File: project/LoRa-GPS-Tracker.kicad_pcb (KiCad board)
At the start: 2 copper layers, 38.9 x 40 mm, 47 parts, among them IC1 MCP73831-2-OT, IC103 FT230XS, IC104 NCP705MT30TCG, IC2 MCP100-300D, M1 SIM28ML, M102 RAK3172, Q101 BSS123, Q102 TP0610K, Q103 BSH205G2VL, SW101 ON / OFF, X1 USB_B_Micro, X103 +, X104 -, X3 Conn_Coaxial

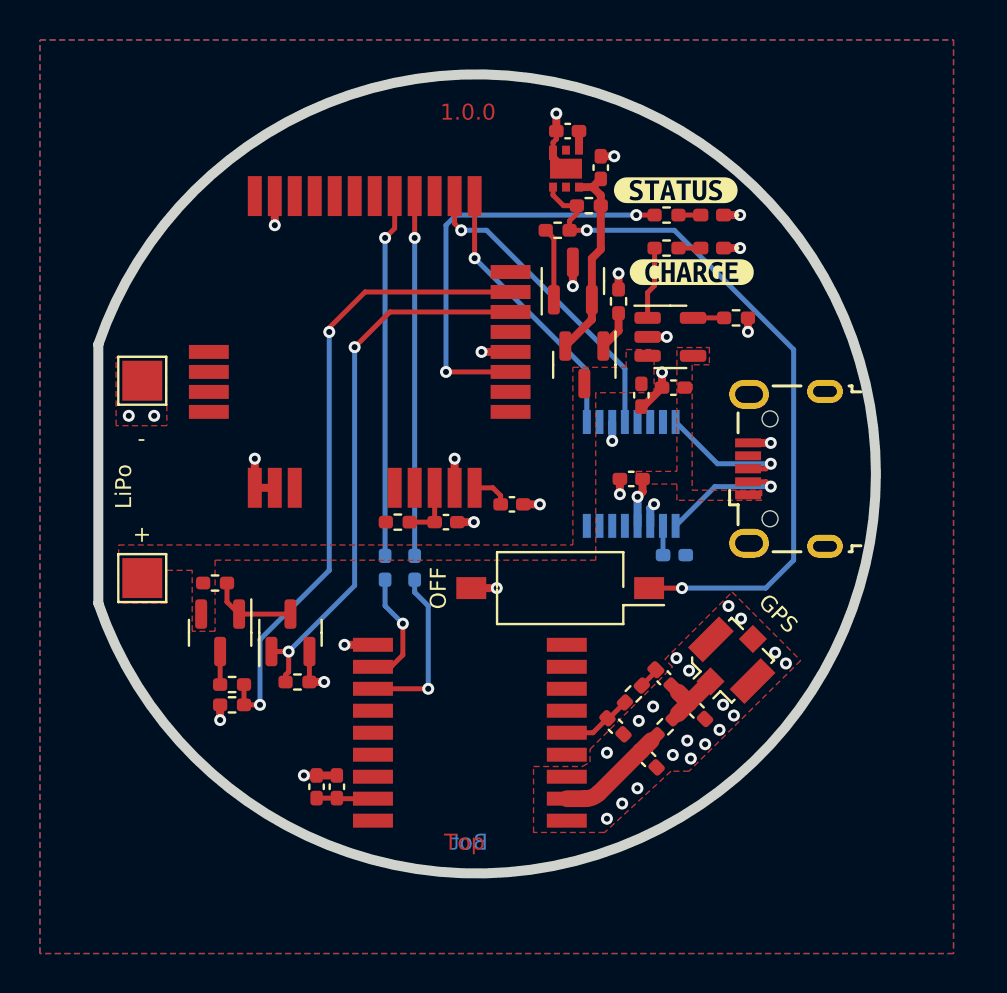
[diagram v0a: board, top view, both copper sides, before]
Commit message: Version 1
PCB:
- Update build.yaml
- Add PCB variant for KiBot

Signed-off-by: Daniel Kampert <DanielKampert@kampis-elektroecke.de>
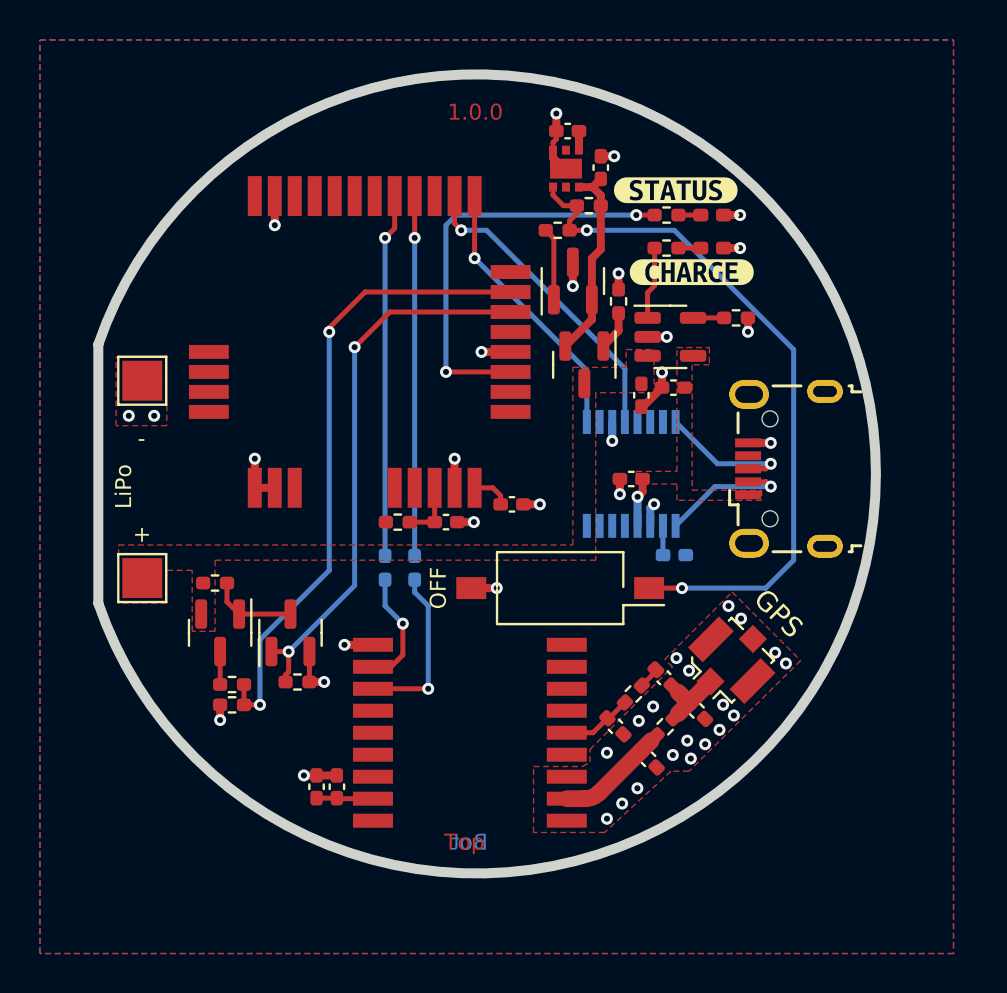
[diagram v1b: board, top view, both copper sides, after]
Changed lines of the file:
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@@
   (paper "A4")
   (title_block
-    (title "LoRa-Weatherstation")
-    (date "2022-12-31")
+    (title "LoRa-GPS-Tracker")
+    (date "2024-01-07")
     (rev "1.0")
     (company "Kampis-Elektroecke")
@@
         (effects (font (size 1 1) (thickness 0.15)))
     )
-    (fp_text user "${REFERENCE}" (at 0 0 90) (layer "F.Fab")
+    (fp_text user "${REFERENCE}" (at 0 0 -180) (layer "F.Fab")
         (effects (font (size 0.32 0.32) (thickness 0.05)))
     )
@@
         (effects (font (size 1 1) (thickness 0.15)))
     )
-    (fp_text user "${REFERENCE}" (at 0 0) (layer "F.Fab")
+    (fp_text user "${REFERENCE}" (at 0 0 90) (layer "F.Fab")
         (effects (font (size 1 1) (thickness 0.15)))
     )
@@
         (effects (font (size 1 1) (thickness 0.15)))
     )
-    (fp_text user "${REFERENCE}" (at 0 0) (layer "F.Fab")
+    (fp_text user "${REFERENCE}" (at 0 0 90) (layer "F.Fab")
         (effects (font (size 0.4 0.4) (thickness 0.06)))
     )
@@
         (effects (font (size 1 1) (thickness 0.15)))
     )
-    (fp_text user "${REFERENCE}" (at 0 0 90) (layer "F.Fab")
+    (fp_text user "${REFERENCE}" (at 0 0 180) (layer "F.Fab")
         (effects (font (size 0.32 0.32) (thickness 0.05)))
     )
@@
         (effects (font (size 1 1) (thickness 0.15)))
     )
-    (fp_text user "${REFERENCE}" (at 0 0 90) (layer "F.Fab")
+    (fp_text user "${REFERENCE}" (at 0 0 -180) (layer "F.Fab")
         (effects (font (size 0.32 0.32) (thickness 0.05)))
     )
@@
         (effects (font (size 1 1) (thickness 0.15)))
     )
-    (fp_text user "${REFERENCE}" (at 0.1 0 180 unlocked) (layer "F.Fab")
+    (fp_text user "${REFERENCE}" (at 0.1 0 unlocked) (layer "F.Fab")
         (effects (font (size 0.6 0.6) (thickness 0.09)))
     )
@@
         (effects (font (size 1 1) (thickness 0.15)))
     )
-    (fp_text user "${REFERENCE}" (at 0 0 90) (layer "F.Fab")
+    (fp_text user "${REFERENCE}" (at 0 0 180) (layer "F.Fab")
         (effects (font (size 0.32 0.32) (thickness 0.05)))
     )
@@
         (effects (font (size 1 1) (thickness 0.15)))
     )
-    (fp_text value "GPS" (at -0.006364 -3.295881 135) (layer "F.SilkS")
-        (effects (font (size 0.8 0.8) (thickness 0.1)))
+    (fp_text value "GPS" (at 0 -3.302 135) (layer "F.SilkS")
+        (effects (font (size 1 1) (thickness 0.15)))
     )
     (fp_text user "${REFERENCE}" (at 0 0 135) (layer "F.Fab")
@@
   (gr_arc (start 124.901 99.72) (mid 163.816029 106.197) (end 124.901 112.674)
     (stroke (width 0.5) (type solid)) (layer "Edge.Cuts"))
-  (gr_text "1.0.0" (at 143.4 88.1) (layer "F.Cu")
+  (gr_text "1.0.0" (at 143.766 88.1) (layer "F.Cu")
     (effects (font (size 0.8 0.8) (thickness 0.12)))
   )

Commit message: Version 1.0
Electronics:
- Add jumper for current measurement
- Add jumper to set the RAK module into bootloader mode
- Add capacitor for battery measurement

Testing Firmware:
- Add UART GPS parser
- SubGHz PHY is now using the coordinates from GPS

Firmware:
- Add STM32CubeMX project

Misc:
- Add README

- Add CHANGELOG

Signed-off-by: Daniel Kampert <DanielKampert@kampis-elektroecke.de>
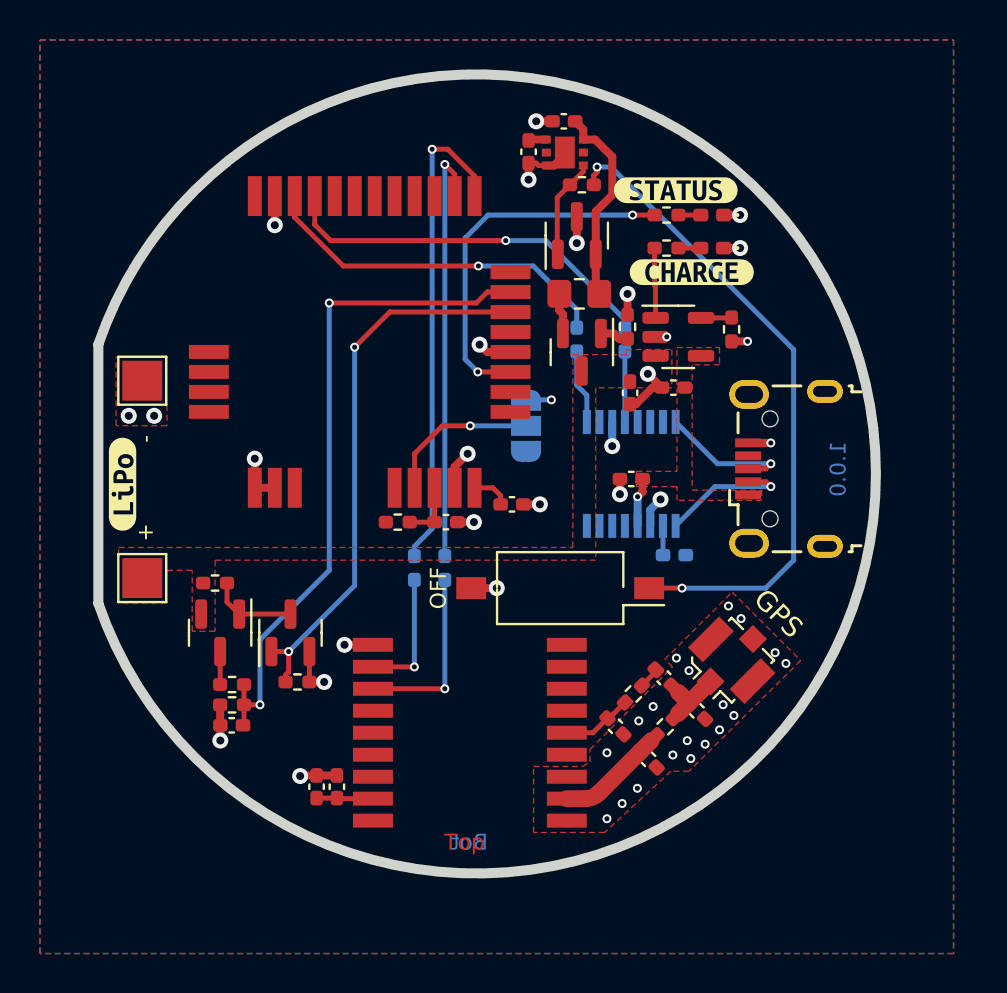
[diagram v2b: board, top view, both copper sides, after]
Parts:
- added C103: 100n, Capacitor_SMD:C_0402_1005Metric_Pad0.74x0.62mm_HandSolder, F.Cu at (131.6, 118.8)
- added JP101: PROG, Jumper:SolderJumper-3_P1.3mm_Open_RoundedPad1.0x1.5mm_NumberLabels, B.Cu at (146.3, 103.8)
- added R114: 0R, Resistor_SMD:R_0402_1005Metric_Pad0.72x0.64mm_HandSolder, B.Cu at (148.8, 99.5)
- added R115: 0R, Resistor_SMD:R_0402_1005Metric_Pad0.72x0.64mm_HandSolder, B.Cu at (151.3, 99.5)
- added kibuzzard-659DAEA0: G***, kibuzzard-659DAEA0, F.Cu at (126.1, 106.7)
- R101, R102: value 100R -> 0R
- R112: value 3k3 -> 0R; footprint Resistor_SMD:R_0402_1005Metric_Pad0.72x0.64mm_HandSolder -> Resistor_SMD:R_0805_2012Metric_Pad1.20x1.40mm_HandSolder
- moved R112 3.36 mm to (149.0, 97.2), turned to 180 degrees
- moved C111 2.96 mm to (148.2, 88.6), turned to 180 degrees
- moved IC2 2.29 mm to (148.8, 94.3)
- moved C112 2.21 mm to (146.4, 90.1), turned to -90 degrees
- moved R102 1.51 mm to (142.2, 110.9)
- moved R101 1.47 mm to (140.7, 110.9)
- moved R111 1.35 mm to (151.4, 98.8)
- moved R113 1.10 mm to (149.1, 91.7), turned to 0 degrees
- moved IC104 0.81 mm to (148.2, 90.1), turned to -90 degrees
- moved Q103 0.64 mm to (149.1, 100.1)
- moved R107 0.62 mm to (156.6, 99.0), turned to -90 degrees
- moved C108 0.58 mm to (151.5, 102.1)
- moved IC1 0.40 mm to (153.9, 99.3)
- renumbered C103 to C104, C104 to C105, C105 to C106, C106 to C107, C107 to C108, C108 to C109, C109 to C110, C110 to C111, C111 to C112, C112 to C113, C113 to C114, R114 to R116, R115 to R117
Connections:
- IC103 pad 1: /Rx_PROG -> Net-(IC103-TXD)
- IC103 pad 4: /Tx_PROG -> Net-(IC103-RXD)
- IC104 pad 4: Net-(IC104-EN) -> Net-(IC102-~{RST})
- M102 pad 1: /Rx_PROG -> /Tx_GNSS
- M102 pad 10: unconnected-(M102-SDA-Pad10) -> /Tx_PROG
- M102 pad 2: /Tx_PROG -> /Rx_GNSS
- M102 pad 21: unconnected-(M102-BOOT-Pad21) -> Net-(JP101-C)
- M102 pad 4: /Rx_GNSS -> unconnected-(M102-TX1-Pad4)
- M102 pad 5: /Tx_GNSS -> unconnected-(M102-RX1-Pad5)
- M102 pad 9: unconnected-(M102-SCL-Pad9) -> /Rx_PROG
- Q103 pad 2: Net-(IC102-VDD) -> Net-(Q103-S)
- R112 pad 1: Net-(IC102-~{RST}) -> Net-(IC102-VDD)
- R112 pad 2: Net-(IC104-EN) -> Net-(Q103-S)
- R113 pad 1: Net-(IC102-VDD) -> Net-(IC102-~{RST})
- R113 pad 2: Net-(IC104-EN) -> Net-(R113-Pad2)
- SW101 pad 1: Net-(IC104-EN) -> Net-(R113-Pad2)
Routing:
- net Net-(IC104-EN): track 35.2 -> 0.00 mm, vias 2 -> 0
- net Net-(R113-Pad2): track 0.00 -> 32.9 mm, vias 0 -> 2
- net Net-(JP101-C): track 0.00 -> 7.86 mm, vias 0 -> 1
- net /Tx_GNSS: track 18.2 -> 24.4 mm
- net /Rx_PROG: track 13.6 -> 19.3 mm
- net Net-(IC103-TXD): track 0.00 -> 3.73 mm
- net Net-(IC103-RXD): track 0.00 -> 3.53 mm
- net /Rx_GNSS: track 18.0 -> 21.4 mm
- net GND: track 29.0 -> 31.9 mm
- net Net-(M102-PB12): track 21.2 -> 18.6 mm
- net /Tx_PROG: track 15.6 -> 18.0 mm
- net Net-(Q103-S): track 0.00 -> 2.06 mm
- net +3V0: track 7.81 -> 9.66 mm, vias 2 -> 3
- net /V_BAT: track 31.9 -> 33.7 mm
- net Net-(IC102-~{RST}): track 3.65 -> 4.99 mm
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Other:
- board text added: "PROG"
- board text removed: "LiPo"

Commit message: Working on version 1:
Hardware:
- Fix empty ZIP files in KiBot template
- Fix missing drill files in KiBot template
- Add optional SWD connector for debugging
- Add minimal variant without UART console and SWD connector

Nucleo Demo:
- Adding Standby mode and wakeup by UART
- Set internal oscillator frequency to 32 MHz to match the external crystal

Signed-off-by: Daniel Kampert <DanielKampert@kampis-elektroecke.de>
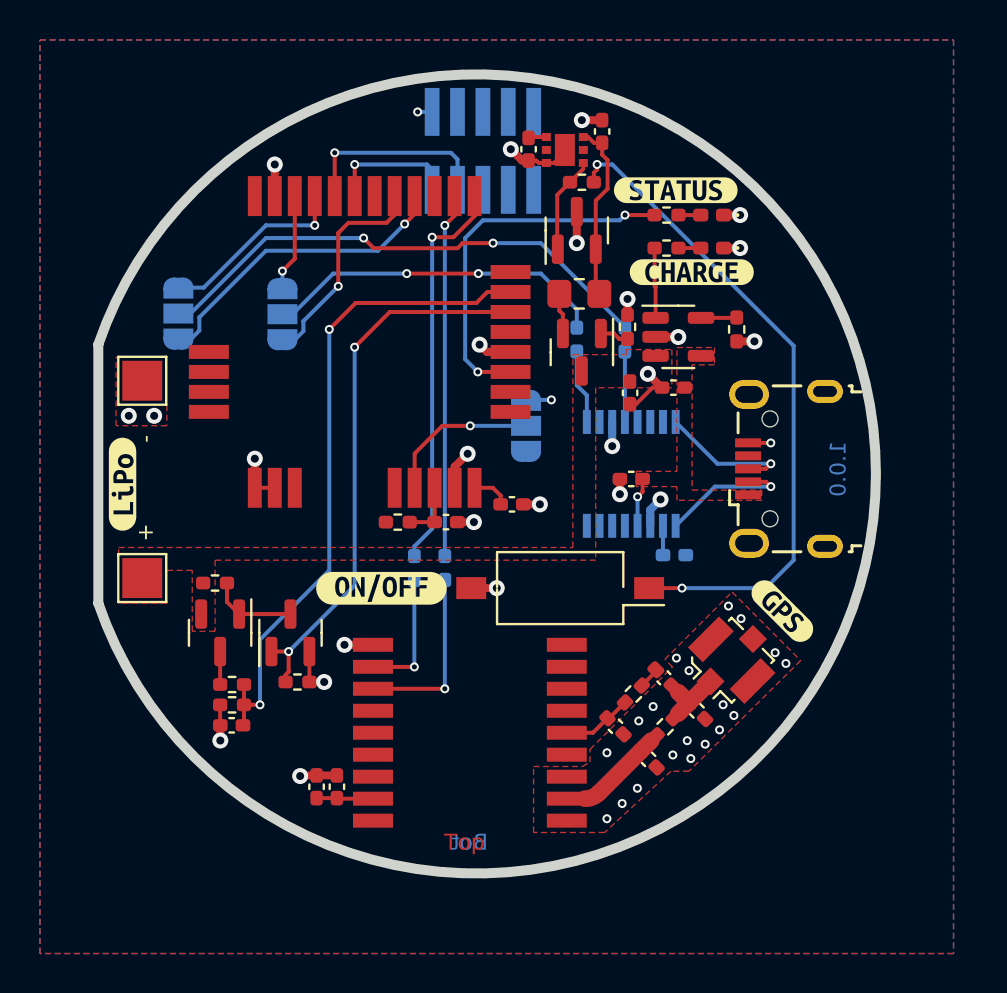
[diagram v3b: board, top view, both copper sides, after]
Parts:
- added JP101: ~, Jumper:SolderJumper-3_P1.3mm_Open_RoundedPad1.0x1.5mm_NumberLabels, B.Cu at (128.9, 98.2)
- added JP102: ~, Jumper:SolderJumper-3_P1.3mm_Open_RoundedPad1.0x1.5mm_NumberLabels, B.Cu at (134.1, 98.2)
- added X105: DEBUG, Samtec:SHF-105-01-L-D-SM-TR, B.Cu at (144.2, 90.0)
- added kibuzzard-65A187C4: G***, kibuzzard-65A187C4, B.Cu at (140.1, 90.5)
- added kibuzzard-65A18804: G***, kibuzzard-65A18804, F.Cu at (159.1, 113.1)
- added kibuzzard-65A18838: G***, kibuzzard-65A18838, F.Cu at (139.1, 111.9)
- moved C111 1.99 mm to (150.1, 89.1), turned to 90 degrees
- moved R107 0.25 mm to (156.8, 99.0)
- moved IC2 0.25 mm to (148.8, 94.0)
- moved R113 0.13 mm to (149.1, 91.6)
- moved C112 0.13 mm to (146.4, 89.9)
- moved IC104 0.13 mm to (148.2, 90.0)
- renumbered JP101 to JP103
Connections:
- M102 pad 4: unconnected-(M102-TX1-Pad4) -> /Rx_LOG
- M102 pad 5: unconnected-(M102-RX1-Pad5) -> /Tx_LOG
- M102 pad 7: unconnected-(M102-SWDIO-Pad7) -> /SWDIO
- M102 pad 8: unconnected-(M102-SWCLK-Pad8) -> /SWDCLK
- R114 pad 1: /Tx_PROG -> /Tx
- R115 pad 2: /Rx_PROG -> /Rx
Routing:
- net /Rx: track 0.00 -> 26.0 mm, vias 0 -> 2
- net /Tx: track 0.00 -> 17.2 mm, vias 0 -> 2
- net /Rx_LOG: track 0.00 -> 15.7 mm, vias 0 -> 1
- net /Tx_PROG: track 18.0 -> 4.87 mm
- net /Tx_LOG: track 0.00 -> 11.0 mm, vias 0 -> 1
- net /SWDCLK: track 0.00 -> 9.97 mm, vias 0 -> 1
- net /Rx_PROG: track 19.3 -> 9.58 mm
- net /SWDIO: track 0.00 -> 6.58 mm, vias 0 -> 1
- net /Tx_GNSS: track 24.4 -> 19.9 mm
- net /Rx_GNSS: track 21.4 -> 18.2 mm
- net GND: track 31.9 -> 33.2 mm
- net Net-(IC102-VDD): track 10.2 -> 9.05 mm
- net /V_BAT: track 33.7 -> 32.9 mm
- net +3V0: track 9.66 -> 10.4 mm, vias 3 -> 4
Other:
- board text removed: "OFF"

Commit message: Update build.yml
Add variants to build.yml

Signed-off-by: Daniel Kampert <DanielKampert@kampis-elektroecke.de>
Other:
- board text added: "0,1250 mm / 0,1250 mm"
- board text added: "0,2500 mm"
- board text added: "1,5 mm"
- board text added: "1,5900 mm"
- board text added: "Blue"
- board text added: "HAL SnPb"
- board text removed: "0,2000 mm / 0,0000 mm"
- board text removed: "0,3000 mm"
- board text removed: "1,51 mm"
- board text removed: "1,6000 mm"
- board text removed: "Green"
- board text removed: "None"

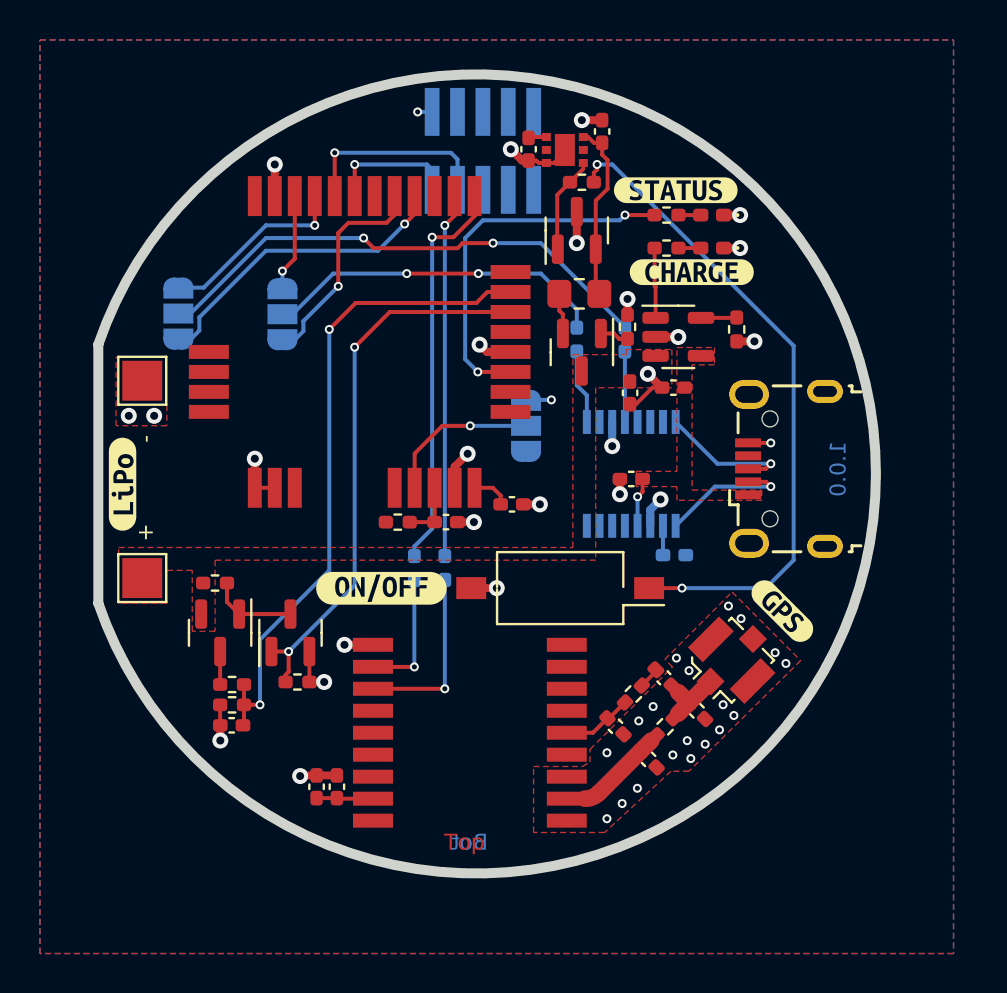
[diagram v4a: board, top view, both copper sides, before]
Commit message: Working on version 1
Hardware:
- Finalize PCB
- Replace expensive components with cheaper ones
- Add GPS antenna
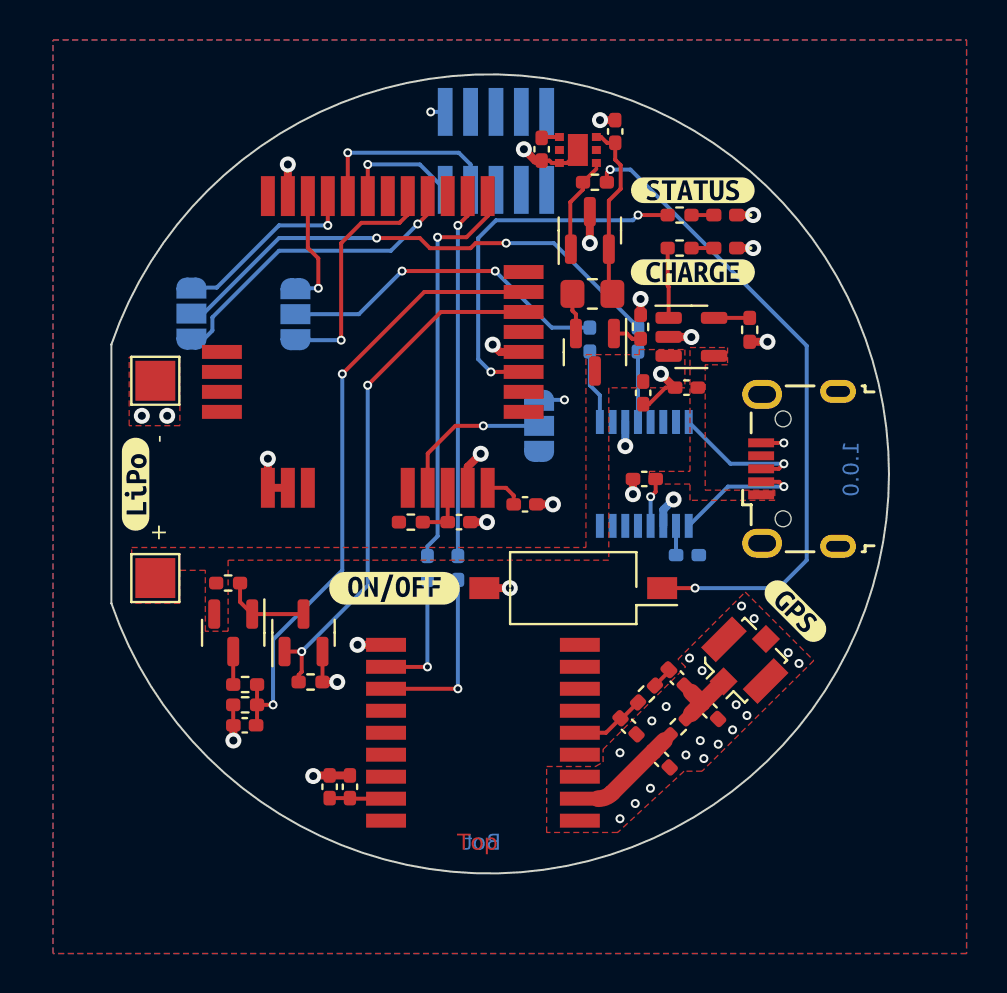
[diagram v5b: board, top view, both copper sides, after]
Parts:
- moved kibuzzard-65985972 0.85 mm to (154.7, 92.0)
- moved R107 0.65 mm to (157.5, 99.0)
- moved C101 0.65 mm to (137.5, 121.9)
- moved C102 0.65 mm to (136.5, 121.9)
- moved C103 0.65 mm to (132.2, 118.8)
- moved C104 0.65 mm to (154.3, 101.9)
- moved C105 0.65 mm to (151.4, 118.8)
- moved C106 0.65 mm to (153.1, 120.5)
- moved C107 0.65 mm to (155.5, 118.1)
- moved C108 0.65 mm to (152.2, 102.1)
- moved C109 0.65 mm to (154.4, 110.3)
- moved C110 0.65 mm to (152.2, 106.5)
- moved C111 0.65 mm to (150.8, 89.1)
- moved C112 0.65 mm to (147.1, 89.9)
- moved C113 0.65 mm to (143.0, 108.6)
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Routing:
- net /V_BAT: track 32.9 -> 31.6 mm
- net /BAT_E: track 27.6 -> 26.5 mm
- net /Tx_PROG: track 4.87 -> 5.97 mm
- net /Tx_LOG: track 11.0 -> 12.0 mm
- net /SWDIO: track 6.58 -> 5.98 mm
